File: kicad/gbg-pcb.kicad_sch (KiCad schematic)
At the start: 49 parts, among them IC2 D78B05T-1.0, J1 12 2.54mm pitch header pins, J12 screw terminal, J2 Conn_01x02, J3 VP0265840000G, J4 Screw_Terminal_01x04, J5 Screw_Terminal_01x03, J8 1017514, J9 1017514, P1 rpi pico 1, Q1 PSMN1R2-25YLDX, Q2 PSMN1R2-25YLDX, Q3 PSMN1R2-25YLDX, Q4 PSMN1R2-25YLDX, SW1 screw terminal, U1 IFX007TAUMA1, U2 IFX007TAUMA1, U3 IFX007TAUMA1, U4 IFX007TAUMA1

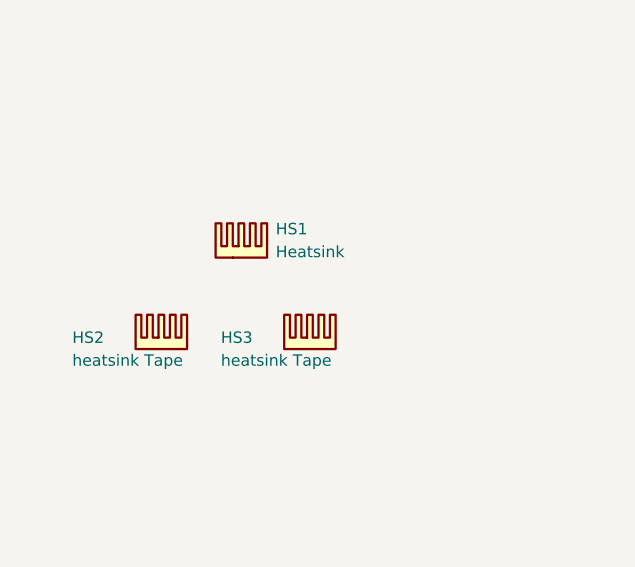
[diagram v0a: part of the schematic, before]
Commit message: different heatsinks
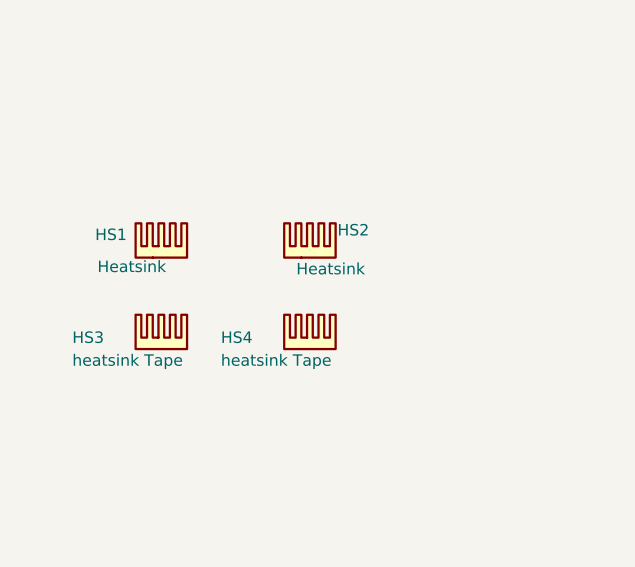
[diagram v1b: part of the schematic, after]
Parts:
- added HS1: Heatsink, kicad libraries:heatsink V2027B, symbol Mechanical:Heatsink
- HS2: renamed from HS1; footprint kicad libraries:SK 582 100 AL -> kicad libraries:heatsink V2027B; Manufacturer_Name Fischer Elektronik -> Assmann WSW Components; Manufacturer_Part_Number SK 582 100 AL -> V2027B; digikey_part_number 5496-SK582100AL-ND -> AE11383-ND; mount_type tht, use HS2 and HS3 to attach, buy in multiples of 10 -> tht; price 1 -> 0.77
- HS3: renamed from HS2; footprint kicad libraries:tape -> kicad libraries:tape_1; Manufacturer_Part_Number TG-T1000-43-20-0.25-5PT -> TG-T1000-24-24-0.25-5PT; digikey_part_number 1168-TG-T1000-43-20-0.25-5PT-ND -> 1168-TG-T1000-24-24-0.25-5PT-ND; price .31 -> 0.31
- HS4: renamed from HS3; footprint kicad libraries:tape -> kicad libraries:tape_1; Manufacturer_Part_Number TG-T1000-43-20-0.25-5PT -> TG-T1000-26-26-0.25-5PT; digikey_part_number 1168-TG-T1000-43-20-0.25-5PT-ND -> 1168-TG-T1000-26-26-0.25-5PT-ND; price .31 -> 0.33
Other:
- moved on the sheet: HS2
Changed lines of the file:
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@@
 	(symbol
 		(lib_id "Mechanical:Heatsink")
-		(at 44.45 234.95 0)
+		(at 52.07 234.95 0)
 		(unit 1)
 		(exclude_from_sim no)
@@
 		(on_board yes)
 		(dnp no)
-		(fields_autoplaced yes)
-		(property "Reference" "HS1"
-			(at 48.26 231.7749 0)
+		(property "Reference" "HS2"
+			(at 55.118 231.902 0)
 			(effects
 				(font
@@
 		)
 		(property "Value" "Heatsink"
-			(at 48.26 234.3149 0)
+			(at 50.546 236.22 0)
 			(effects
 				(font
@@
 			)
 		)
-		(property "Footprint" "kicad libraries:SK 582 100 AL"
-			(at 44.7548 234.95 0)
+		(property "Footprint" "kicad libraries:heatsink V2027B"
+			(at 52.3748 234.95 0)
 			(effects
 				(font
@@
 			)
 		)
-		(property "Datasheet" "https://www.digikey.com/en/products/detail/fischer-elektronik/SK-582-100-AL/25827171"
-			(at 44.7548 234.95 0)
+		(property "Datasheet" "https://www.digikey.com/en/products/detail/assmann-wsw-components/V2027B/8826896"
+			(at 52.3748 234.95 0)
 			(effects
 				(font
@@
 		)
 		(property "Description" "Heatsink"
-			(at 44.45 234.95 0)
+			(at 52.07 234.95 0)
 			(effects
 				(font
@@
 			)
 		)
-		(property "Manufacturer_Name" "Fischer Elektronik"
-			(at 44.45 234.95 0)
+		(property "Manufacturer_Name" "Assmann WSW Components"
+			(at 52.07 234.95 0)
 			(effects
 				(font
@@
 			)
 		)
-		(property "Manufacturer_Part_Number" "SK 582 100 AL"
-			(at 44.45 234.95 0)
+		(property "Manufacturer_Part_Number" "V2027B"
+			(at 52.07 234.95 0)
 			(effects
 				(font
@@
 			)
 		)
-		(property "digikey_part_number" "5496-SK582100AL-ND"
-			(at 44.45 234.95 0)
+		(property "digikey_part_number" "AE11383-ND"
+			(at 52.07 234.95 0)
 			(effects
 				(font
@@
 			)
 		)
-		(property "mount_type" "tht, use HS2 and HS3 to attach, buy in multiples of 10"
-			(at 44.45 234.95 0)
+		(property "mount_type" "tht"
+			(at 52.07 234.95 0)
 			(effects
 				(font
@@
 			)
 		)
-		(property "price" "1"
-			(at 44.45 234.95 0)
+		(property "price" "0.77"
+			(at 52.07 234.95 0)
 			(effects
 				(font
@@
 			(project ""
 				(path "/3bb9adb4-655f-45ab-af84-44b563241ee2"
-					(reference "HS1")
+					(reference "HS2")
 					(unit 1)
 				)
@@
 		(on_board yes)
 		(dnp no)
-		(property "Reference" "HS2"
+		(property "Reference" "HS3"
 			(at 25.654 243.84 0)
 			(effects
@@
 			)
 		)
-		(property "Footprint" "kicad libraries:tape"
+		(property "Footprint" "kicad libraries:tape_1"
 			(at 35.8648 245.11 0)
 			(effects
@@
 			)
 		)
-		(property "Datasheet" "https://www.digikey.com/en/products/detail/t-global-technology/TG-T1000-43-20-0-25-5PT/13919483"
+		(property "Datasheet" "https://www.digikey.com/en/products/detail/t-global-technology/TG-T1000-24-24-0-25-5PT/13919475"
 			(at 35.8648 245.11 0)
 			(effects
@@
 			)
 		)
-		(property "Description" "thermally conductive tape"
+		(property "Description" "heatsink Tape - alternate: 1168-TG-T1000-26-26-0.25-5PT-ND"
 			(at 35.56 245.11 0)
 			(effects
@@
 			)
 		)
-		(property "Manufacturer_Part_Number" "TG-T1000-43-20-0.25-5PT"
+		(property "Manufacturer_Part_Number" "TG-T1000-24-24-0.25-5PT"
 			(at 35.56 245.11 0)
 			(effects
@@
 			)
 		)
-		(property "digikey_part_number" "1168-TG-T1000-43-20-0.25-5PT-ND"
+		(property "digikey_part_number" "1168-TG-T1000-24-24-0.25-5PT-ND"
 			(at 35.56 245.11 0)
 			(effects
@@
 			)
 		)
-		(property "price" ".31"
+		(property "price" "0.31"
 			(at 35.56 245.11 0)
 			(effects
@@
 			(project ""
 				(path "/3bb9adb4-655f-45ab-af84-44b563241ee2"
-					(reference "HS2")
+					(reference "HS3")
 					(unit 1)
 				)
@@
 	)
 	(symbol
+		(lib_id "Mechanical:Heatsink")
+		(at 35.56 234.95 0)
+		(unit 1)
+		(exclude_from_sim no)
+		(in_bom yes)
+		(on_board yes)
+		(dnp no)
+		(property "Reference" "HS1"
+			(at 28.194 232.41 0)
+			(effects
+				(font
+					(size 1.27 1.27)
+				)
+				(justify left)
+			)
+		)
+		(property "Value" "Heatsink"
+			(at 28.448 235.966 0)
+			(effects
+				(font
+					(size 1.27 1.27)
+				)
+				(justify left)
+			)
+		)
+		(property "Footprint" "kicad libraries:heatsink V2027B"
+			(at 35.8648 234.95 0)
+			(effects
+				(font
+					(size 1.27 1.27)
+				)
+				(hide yes)
+			)
+		)
+		(property "Datasheet" "https://www.digikey.com/en/products/detail/assmann-wsw-components/V2027B/8826896"
+			(at 35.8648 234.95 0)
+			(effects
+				(font
+					(size 1.27 1.27)
+				)
+				(hide yes)
+			)
+		)
+		(property "Description" "Heatsink"
+			(at 35.56 234.95 0)
+			(effects
+				(font
+					(size 1.27 1.27)
+				)
+				(hide yes)
+			)
+		)
+		(property "Manufacturer_Name" "Assmann WSW Components"
+			(at 35.56 234.95 0)
+			(effects
+				(font
+					(size 1.27 1.27)
+				)
+				(hide yes)
+			)
+		)
+		(property "Manufacturer_Part_Number" "V2027B"
+			(at 35.56 234.95 0)
+			(effects
+				(font
+					(size 1.27 1.27)
+				)
+				(hide yes)
+			)
+		)
+		(property "digikey_part_number" "AE11383-ND"
+			(at 35.56 234.95 0)
+			(effects
+				(font
+					(size 1.27 1.27)
+				)
+				(hide yes)
+			)
+		)
+		(property "mount_type" "tht"
+			(at 35.56 234.95 0)
+			(effects
+				(font
+					(size 1.27 1.27)
+				)
+				(hide yes)
+			)
+		)
+		(property "price" "0.77"
+			(at 35.56 234.95 0)
+			(effects
+				(font
+					(size 1.27 1.27)
+				)
+				(hide yes)
+			)
+		)
+		(instances
+			(project "gbg-pcb"
+				(path "/3bb9adb4-655f-45ab-af84-44b563241ee2"
+					(reference "HS1")
+					(unit 1)
+				)
+			)
+		)
+	)
+	(symbol
 		(lib_id "Connector:Screw_Terminal_01x04")
 		(at 142.24 81.28 0)
@@
 		(on_board yes)
 		(dnp no)
-		(property "Reference" "HS3"
+		(property "Reference" "HS4"
 			(at 42.164 243.84 0)
 			(effects
@@
 			)
 		)
-		(property "Footprint" "kicad libraries:tape"
+		(property "Footprint" "kicad libraries:tape_1"
 			(at 52.3748 245.11 0)
 			(effects
@@
 			)
 		)
-		(property "Datasheet" "https://www.digikey.com/en/products/detail/t-global-technology/TG-T1000-43-20-0-25-5PT/13919483"
+		(property "Datasheet" "https://www.digikey.com/en/products/detail/t-global-technology/TG-T1000-26-26-0-25-5PT/13919488"
 			(at 52.3748 245.11 0)
 			(effects
@@
 			)
 		)
-		(property "Description" "thermally conductive tape"
+		(property "Description" "heatsink Tape"
 			(at 52.07 245.11 0)
 			(effects
@@
 			)
 		)
-		(property "Manufacturer_Part_Number" "TG-T1000-43-20-0.25-5PT"
+		(property "Manufacturer_Part_Number" "TG-T1000-26-26-0.25-5PT"
 			(at 52.07 245.11 0)
 			(effects
@@
 			)
 		)
-		(property "digikey_part_number" "1168-TG-T1000-43-20-0.25-5PT-ND"
+		(property "digikey_part_number" "1168-TG-T1000-26-26-0.25-5PT-ND"
 			(at 52.07 245.11 0)
 			(effects
@@
 			)
 		)
-		(property "price" ".31"
+		(property "price" "0.33"
 			(at 52.07 245.11 0)
 			(effects
@@
 			(project "gbg-pcb"
 				(path "/3bb9adb4-655f-45ab-af84-44b563241ee2"
-					(reference "HS3")
+					(reference "HS4")
 					(unit 1)
 				)

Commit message: adjust heatsink
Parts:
- HS4: Manufacturer_Part_Number TG-T1000-26-26-0.25-5PT -> TG-T1000-24-24-0.25-5PT; digikey_part_number 1168-TG-T1000-26-26-0.25-5PT-ND -> 1168-TG-T1000-24-24-0.25-5PT-ND; price 0.33 -> 0.31
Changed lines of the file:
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@@
 			)
 		)
-		(property "Description" "heatsink Tape"
+		(property "Description" "heatsink Tape - alternate: 1168-TG-T1000-26-26-0.25-5PT-ND"
 			(at 52.07 245.11 0)
 			(effects
@@
 			)
 		)
-		(property "Manufacturer_Part_Number" "TG-T1000-26-26-0.25-5PT"
+		(property "Manufacturer_Part_Number" "TG-T1000-24-24-0.25-5PT"
 			(at 52.07 245.11 0)
 			(effects
@@
 			)
 		)
-		(property "digikey_part_number" "1168-TG-T1000-26-26-0.25-5PT-ND"
+		(property "digikey_part_number" "1168-TG-T1000-24-24-0.25-5PT-ND"
 			(at 52.07 245.11 0)
 			(effects
@@
 			)
 		)
-		(property "price" "0.33"
+		(property "price" "0.31"
 			(at 52.07 245.11 0)
 			(effects

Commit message: change pcb to use 26mm thermal tape and start instructions
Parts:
- HS3, HS4: Manufacturer_Part_Number TG-T1000-24-24-0.25-5PT -> TG-T1000-26-26-0.25-5PT; digikey_part_number 1168-TG-T1000-24-24-0.25-5PT-ND -> 1168-TG-T1000-26-26-0.25-5PT-ND; price 0.31 -> .33
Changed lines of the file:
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@@
 			)
 		)
-		(property "Datasheet" "https://www.digikey.com/en/products/detail/t-global-technology/TG-T1000-24-24-0-25-5PT/13919475"
+		(property "Datasheet" "https://www.digikey.com/en/products/detail/t-global-technology/TG-T1000-26-26-0-25-5PT/13919488"
 			(at 35.8648 245.11 0)
 			(effects
@@
 			)
 		)
-		(property "Description" "heatsink Tape - alternate: 1168-TG-T1000-26-26-0.25-5PT-ND"
+		(property "Description" "heatsink tape"
 			(at 35.56 245.11 0)
 			(effects
@@
 			)
 		)
-		(property "Manufacturer_Part_Number" "TG-T1000-24-24-0.25-5PT"
+		(property "Manufacturer_Part_Number" "TG-T1000-26-26-0.25-5PT"
 			(at 35.56 245.11 0)
 			(effects
@@
 			)
 		)
-		(property "digikey_part_number" "1168-TG-T1000-24-24-0.25-5PT-ND"
+		(property "digikey_part_number" "1168-TG-T1000-26-26-0.25-5PT-ND"
 			(at 35.56 245.11 0)
 			(effects
@@
 			)
 		)
-		(property "price" "0.31"
+		(property "price" ".33"
 			(at 35.56 245.11 0)
 			(effects
@@
 			)
 		)
-		(property "Description" "heatsink Tape - alternate: 1168-TG-T1000-26-26-0.25-5PT-ND"
+		(property "Description" "heatsink tape"
 			(at 52.07 245.11 0)
 			(effects
@@
 			)
 		)
-		(property "Manufacturer_Part_Number" "TG-T1000-24-24-0.25-5PT"
+		(property "Manufacturer_Part_Number" "TG-T1000-26-26-0.25-5PT"
 			(at 52.07 245.11 0)
 			(effects
@@
 			)
 		)
-		(property "digikey_part_number" "1168-TG-T1000-24-24-0.25-5PT-ND"
+		(property "digikey_part_number" "1168-TG-T1000-26-26-0.25-5PT-ND"
 			(at 52.07 245.11 0)
 			(effects
@@
 			)
 		)
-		(property "price" "0.31"
+		(property "price" ".33"
 			(at 52.07 245.11 0)
 			(effects

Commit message: starting pcb layout
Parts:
- removed 5V1, VBat1: green, LED_THT:LED_D3.0mm, symbol Device:LED
- removed B1, B2, B3, B4: STX-3000, kicad libraries:STX-3000_KYC, symbol library:STX-3000
- removed C10, C9: 22 uF, Capacitor_SMD:C_1206_3216Metric_Pad1.33x1.80mm_HandSolder, symbol Device:C
- removed C3, C5: 1000uF, kicad libraries:CP_Radial_D10.0mm_P5.00mm, symbol Device:C_Polarized
- removed C4: 220nF, Capacitor_SMD:C_1206_3216Metric_Pad1.33x1.80mm_HandSolder, symbol Device:C
- removed IC2: D78B05T-1.0, kicad libraries:D78B05T-1.0, symbol Converter_DCDC:OKI-78SR-12_1.0-W36-C
- removed J3: VP0265840000G, kicad libraries:CONN04_VP026584_20P32X18P3_AMP, symbol library:VP0265840000G
- removed J8, J9: 1017514, kicad libraries:PHOENIX_1017514, symbol library:1017514
- removed Q1, Q3: PSMN1R2-25YLDX, Package_TO_SOT_SMD:LFPAK56, symbol Simulation_SPICE:NMOS
- removed R1: 100, Resistor_SMD:R_1206_3216Metric_Pad1.30x1.75mm_HandSolder, symbol Device:R
- removed U1, U2, U3, U4: IFX007TAUMA1, kicad libraries:PG-TO263-7-1_INF, symbol library:IFX007TAUMA1
- added B1, B2, B3, B4: ASJ-200-B-HT, ASJ200BHT, symbol library:ASJ-200-B-HT
- added C1, C2: 0.1uF, Capacitor_SMD:C_0603_1608Metric_Pad1.08x0.95mm_HandSolder, symbol Device:C
- added C3: 1uF, Capacitor_SMD:C_1206_3216Metric, symbol Device:C
- added C4, C5: 33uf, kicad libraries:CAP_KK-8x8_KEM, symbol library:A759KC276M1JAAE054
- added D3: 18V zener, Diode_SMD:D_SOD-123F, symbol Device:D_Zener
- added J5: VP0265840000G, kicad libraries:CONN04_VP026584_20P32X18P3_AMP, symbol library:VP0265840000G
- added J7, J8: 1017491, kicad libraries:CONN_1017491, symbol library:1017491
- added L1: 27 uH, kicad libraries:IND_VLCF4020T-270MR48, symbol Device:L
- added R4: 590k, Resistor_SMD:R_0805_2012Metric_Pad1.20x1.40mm_HandSolder, symbol Device:R
- added R6: 8.2k, Resistor_SMD:R_0805_2012Metric_Pad1.20x1.40mm_HandSolder, symbol Device:R
- added R8: 100k, Resistor_SMD:R_0805_2012Metric_Pad1.20x1.40mm_HandSolder, symbol Device:R
- added R9: 13.7k, Resistor_SMD:R_0805_2012Metric_Pad1.20x1.40mm_HandSolder, symbol Device:R
- added U1, U2: DRV8245HQPWPRQ1, kicad libraries:HTSSOP28_PWP_TEX, symbol library:DRV8245HQPWPRQ1
- added U3: TPS54202HDDCR, kicad libraries:SOT95P280X110-6N tps54202HDDCR, symbol library:TPS54202HDDCR
- C6: value 220nF -> 0.1uF; footprint Capacitor_SMD:C_1206_3216Metric_Pad1.33x1.80mm_HandSolder -> Capacitor_SMD:C_0603_1608Metric_Pad1.08x0.95mm_HandSolder; Manufacturer_Name Samsung Electro-Mechanics -> TDK Corporation; Manufacturer_Part_Number CL31B224KBFNNNE -> CGA3E2X7R1H104K080AA; digikey_part_number 1276-1106-1-ND -> 445-5666-1-ND; price 0.03 -> .044
- C7: value 220nF -> 56pF; footprint Capacitor_SMD:C_1206_3216Metric_Pad1.33x1.80mm_HandSolder -> Capacitor_SMD:C_0603_1608Metric_Pad1.08x0.95mm_HandSolder; Manufacturer_Name Samsung Electro-Mechanics -> Yageo; Manufacturer_Part_Number CL31B224KBFNNNE -> CC0603JRNPO9BN560; digikey_part_number 1276-1106-1-ND -> 311-1066-1-ND; price 0.03 -> .03
- C8: value 220nF -> 47uF; footprint Capacitor_SMD:C_1206_3216Metric_Pad1.33x1.80mm_HandSolder -> Capacitor_SMD:C_1210_3225Metric_Pad1.33x2.70mm_HandSolder; Manufacturer_Name Samsung Electro-Mechanics -> MuRata; Manufacturer_Part_Number CL31B224KBFNNNE -> GRM32ER71A476KE15L; digikey_part_number 1276-1106-1-ND -> 490-5312-1-ND; price 0.03 -> .61
- D13: footprint LED_THT:LED_D5.0mm_Clear -> LED_THT:LED_D5.0mm; price 0.36 -> .13
- HS1: price 0.77 -> .86
- HS2: renamed from HS3; price .33 -> .29
- HS3: renamed from HS2; price 0.77 -> .86
- HS4: price .33 -> .29
- J3: renamed from J4; value Screw_Terminal_01x04 -> joystick; footprint kicad libraries:TerminalBlock_Phoenix_MKDS-1,5-4-5.08_1x04_P5.08mm_Horizontal -> (none); Manufacturer_Name On Shore Technology Inc. -> Amphenol Anytek; Manufacturer_Part_Number OSTTC042162 -> TC0403620000G; digikey_part_number ED2611-ND -> TC0403620000G-ND; price 0.8 -> .47
- J4: renamed from J5; value Screw_Terminal_01x03 -> speed knob; footprint kicad libraries:TerminalBlock_Phoenix_MKDS-1,5-3-5.08_1x03_P5.08mm_Horizontal -> kicad libraries:SAMESKY_TB0011-350-03GR; Manufacturer_Name On Shore Technology Inc. -> Same Sky (Formerly CUI Devices); Manufacturer_Part_Number OSTTC032162 -> TB0011-350-03GR; digikey_part_number ED2610-ND -> 2223-TB0011-350-03GR-ND; price 0.6 -> .44
- J6: renamed from J12; footprint kicad libraries:CONN_OSTTC022162_OST -> (none); Manufacturer_Name On Shore Technology Inc. -> Adam Tech; Manufacturer_Part_Number OSTTC022162 -> EBBA-02-C-SS-BU; digikey_part_number ED2609-ND -> 2057-EBBA-02-C-SS-BU-ND; price 0.43 -> .25
- P1: footprint kicad libraries:MODULE_SC0918 -> Module:RaspberryPi_Pico_Common_SMD
- Q1: renamed from Q2; price 0.74 -> 1.36
- Q2: renamed from Q4; price 0.74 -> 1.36
- R1: renamed from R4; footprint Resistor_SMD:R_1206_3216Metric_Pad1.30x1.75mm_HandSolder -> Resistor_SMD:R_0805_2012Metric_Pad1.20x1.40mm_HandSolder; Manufacturer_Name YAGEO -> Vishay Dale; Manufacturer_Part_Number RC1206JR-13220RL -> CRCW0805220RJNEA; digikey_part_number 13-RC1206JR-13220RLCT-ND -> 541-220ACT-ND; price 0.02 -> .04
- R2: value 2.2k -> 220; footprint Resistor_SMD:R_1206_3216Metric_Pad1.30x1.75mm_HandSolder -> Resistor_SMD:R_0805_2012Metric_Pad1.20x1.40mm_HandSolder; Manufacturer_Name YAGEO -> Vishay Dale; Manufacturer_Part_Number RC1206JR-132K2L -> CRCW0805220RJNEA; digikey_part_number 13-RC1206JR-132K2LCT-ND -> 541-220ACT-ND; price 0.0122 -> .04
- R3, R7: value 680 -> 8.2k; footprint Resistor_SMD:R_1206_3216Metric_Pad1.30x1.75mm_HandSolder -> Resistor_SMD:R_0805_2012Metric_Pad1.20x1.40mm_HandSolder; Manufacturer_Name YAGEO -> Vishay Dale; Manufacturer_Part_Number RC1206FR-07680RL -> CRCW08058K20JNEA; digikey_part_number 311-680FRCT-ND -> 541-8.2KACT-ND; price 0.0133 -> .04
- R5: value 2.2k -> 590k; footprint Resistor_SMD:R_1206_3216Metric_Pad1.30x1.75mm_HandSolder -> Resistor_SMD:R_0805_2012Metric_Pad1.20x1.40mm_HandSolder; Manufacturer_Name YAGEO -> Vishay Dale; Manufacturer_Part_Number RC1206JR-132K2L -> CRCW0805590KFKEA; digikey_part_number 13-RC1206JR-132K2LCT-ND -> 541-590KCCT-ND; price 0.0122 -> .04
- SW1: footprint kicad libraries:CONN_OSTTC022162_OST -> (none); Manufacturer_Name On Shore Technology Inc. -> Adam Tech; Manufacturer_Part_Number OSTTC022162 -> EBBA-02-C-SS-BU; digikey_part_number ED2609-ND -> 2057-EBBA-02-C-SS-BU-ND; price 0.43 -> .25
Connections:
- net +BATT: now also R3.2, R5.1, C1.1, C2.1, C3.1, C4.1, C5.1, J5.3, J5.4, U1.21 (VM), U1.22 (VM), U1.23 (VM), U1.6 (VM), U1.7 (VM), U1.8 (VM), U2.21 (VM), U2.22 (VM), U2.23 (VM), U2.6 (VM), U2.7 (VM), U2.8 (VM), U3.3 (VIN); no longer C6.1, C7.1, C8.1, Q1.4 (G), SW1.1 (A)
- net 5V: now also C7.1, C8.1, L1.2, R8.1
- net GND: now also R7.1, B1.1, B1.3, B1.4, B2.1, B2.3, B2.4, B3.1, B3.3, B3.4, B4.1, B4.3, B4.4, C1.2, C2.2, C3.2, C4.2, C5.2, R6.1, R9.2, U1.12 (GND), U1.13 (GND), U1.14 (GND), U1.15 (GND), U1.16 (GND), U1.17 (GND), U1.28 (ITRIP), U1.5 (DRVOFF), U1.EPAD, U2.12 (GND), U2.13 (GND), U2.14 (GND), U2.15 (GND), U2.16 (GND), U2.17 (GND), U2.28 (ITRIP), U2.5 (DRVOFF), U2.EPAD, U3.1 (GND); no longer C6.2, C7.2, R3.2
- net bt1: now also B1.2
- net bt2: now also B2.2
- net bt3: now also B3.2
- net bt4: now also B4.2
- net left_1: now also U1.3 (PH/IN2)
- net left_2: now also U1.4 (EN/IN1)
- net left_en: now also U1.24 (NSLEEP)
- net right_1: now also U2.3 (PH/IN2)
- net right_2: now also U2.4 (EN/IN1)
- net right_en: now also U2.24 (NSLEEP)
- net at R3.1: now also Q1.4 (G), SW1.2 (B), D3.1 (K)
- net at D13.1 (K): now also R2.1
- net at Q1.5 (D): now also J5.1, J5.2
- net at Q1.1 (S), Q1.2 (S), Q1.3 (S)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: now also D3.2 (A), R4.1; no longer R5.2
- new net: J7.1, J7.2, U1.18 (OUT2), U1.19 (OUT2), U1.20 (OUT2)
- new net: J7.3, J7.4, U1.10 (OUT1), U1.11 (OUT1), U1.9 (OUT1)
- new net: J8.1, J8.2, U2.10 (OUT1), U2.11 (OUT1), U2.9 (OUT1)
- new net: J8.3, J8.4, U2.18 (OUT2), U2.19 (OUT2), U2.20 (OUT2)
- new net: R6.2, U2.27 (MODE)
- new net: C7.2, R8.2, R9.1, U3.4 (FB)
- new net: R5.2, U3.5 (EN)
- new net: R7.2, U1.27 (MODE)
- new net: Q2.4 (G), R4.2, SW1.1 (A)
- new net: C6.1, L1.1, U3.2 (SW)
- new net: C6.2, U3.6 (BOOT)
- no-connect marks 12 -> 10
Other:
- note added: "+"
- note added: "1.8-5.5v"
- note added: "8.2k +-10% LVL2 INDEPENDENT"
- note added: "LVL6, in independent mode that means faults are retried"
- note removed: "left"
- note removed: "right"
- moved on the sheet: 3V1, HS3, HS4, J4, J6, Q1, Q2, R1, SW1

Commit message: working on layout
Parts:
- J3: footprint (none) -> kicad libraries:TC0403620000G
- J5: value VP0265840000G -> screw terminal; Manufacturer_Name (none) -> Amphenol Anytek; Manufacturer_Part_Number (none) -> VP0265840000G; digikey_part_number (none) -> 1818-VP0265840000G-ND; mount_type (none) -> tht; price (none) -> 2.04
- J6, SW1: footprint (none) -> kicad libraries:EBBA-02-C-SS-BU
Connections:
- net +BATT: no longer J5.4
- net at J5.1, Q1.5 (D): no longer J5.2
- no-connect marks 10 -> 12
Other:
- moved on the sheet: B1, B2, B3, B4, D3, J5, J6, Q1, Q2, R3, R4, SW1

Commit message: arrange
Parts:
- removed J5: screw terminal, kicad libraries:CONN04_VP026584_20P32X18P3_AMP, symbol library:VP0265840000G
- added J5: TB005-762-02BE, kicad libraries:CUI_TB005-762-02BE, symbol Connector:Screw_Terminal_01x02
- C8: footprint Capacitor_SMD:C_1210_3225Metric_Pad1.33x2.70mm_HandSolder -> Capacitor_SMD:C_1206_3216Metric_Pad1.33x1.80mm_HandSolder; Manufacturer_Part_Number GRM32ER71A476KE15L -> GRM31CR71E106KA12L; digikey_part_number 490-5312-1-ND -> 490-6518-1-ND; price .61 -> .19
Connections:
- net +3.3V: now also R1.1; no longer 3V1.2 (A)
- net +BATT: now also J5.2 (Pin_2)
- net GND: now also 3V1.1 (K), D13.1 (K); no longer R1.2, R2.2
- net at R2.1: now also P1.17 (GP13); no longer D13.1 (K)
- net at D13.2 (A): now also R2.2; no longer P1.17 (GP13)
- net at Q1.5 (D): now also J5.1 (Pin_1)
- new net: 3V1.2 (A), R1.2
- no-connect marks 12 -> 10
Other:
- note added: "A114159-ND"
- moved on the sheet: 3V1, D13, R1, R2

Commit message: work on layout
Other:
- note added: "TODO: weelye compatible tabs?"
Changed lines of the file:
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@@
 	(text "A114159-ND"
 		(exclude_from_sim no)
-		(at 268.986 100.33 0)
+		(at 367.284 38.354 0)
 		(effects
 			(font
@@
 		)
 	)
+	(text "TODO: \nweelye compatible tabs?"
+		(exclude_from_sim no)
+		(at 387.604 37.592 0)
+		(effects
+			(font
+				(size 1.27 1.27)
+			)
+		)
+	)
 	(text "A114159-ND"
 		(exclude_from_sim no)
-		(at 269.24 102.362 0)
+		(at 367.538 40.386 0)
 		(effects
 			(font
@@
 		(property "Reference" "3V1"
 			(at 96.52 173.0374 90)
+			(show_name yes)
 			(effects
 				(font
